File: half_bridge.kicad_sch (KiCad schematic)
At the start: 26 parts, among them Q1 IGC025S08S1, Q2 IGC025S08S1, U16 SN74LVC1G66DCKR, U4 AD8418, U5 LMG1205YFXR, U6 SN74LVC1G66DCKR

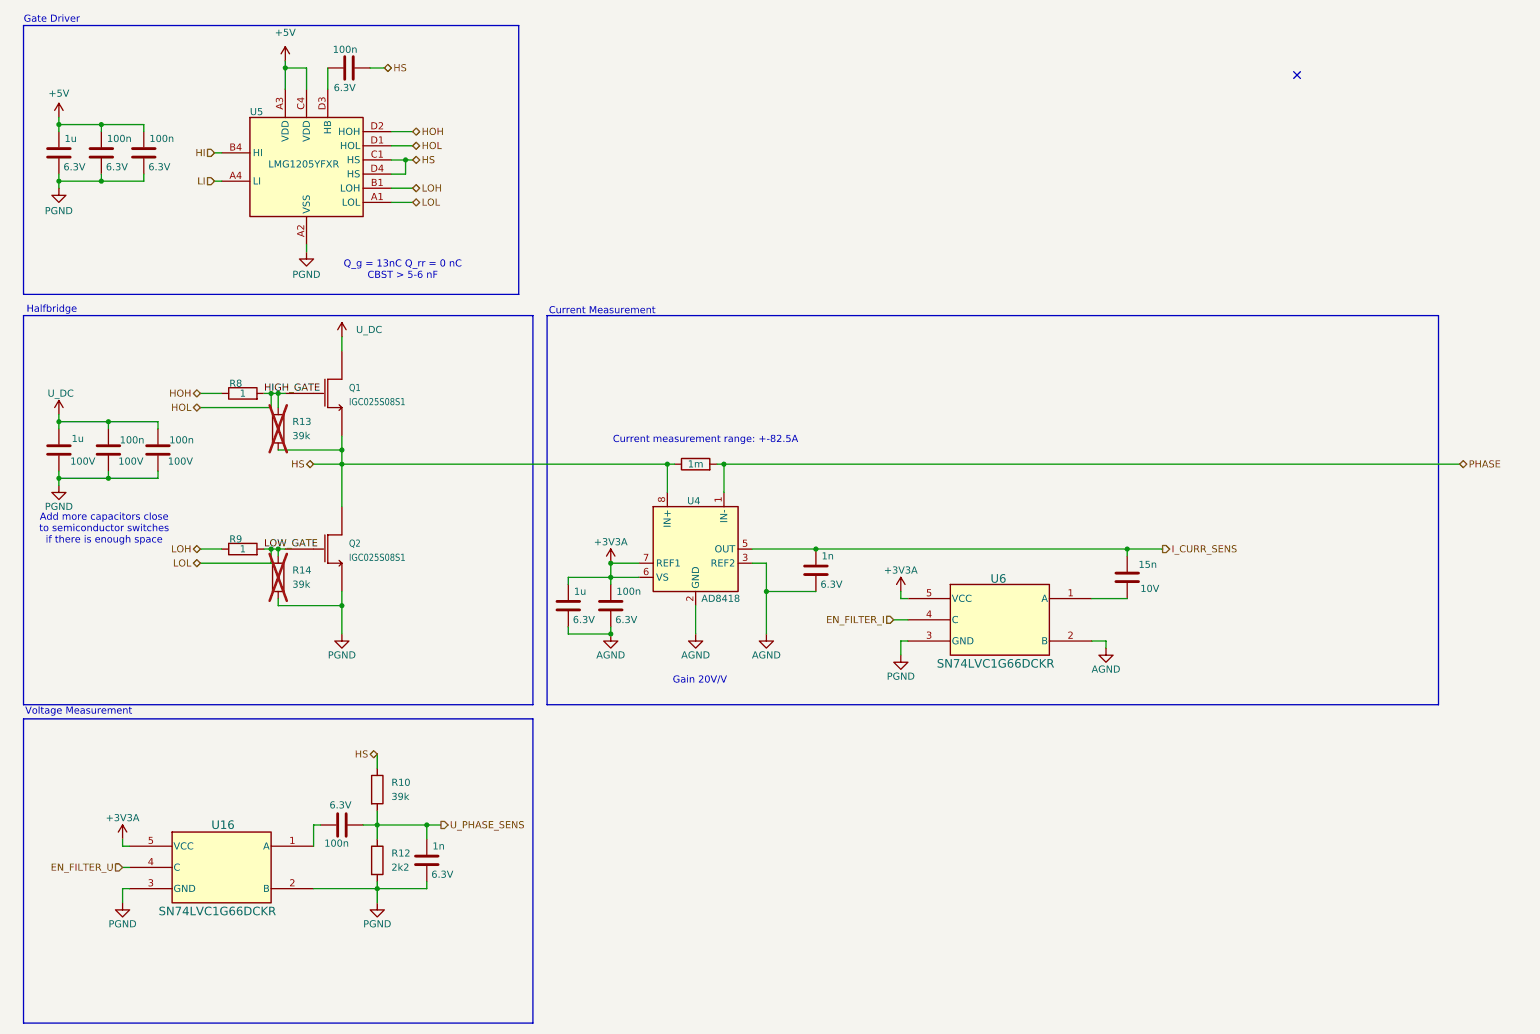
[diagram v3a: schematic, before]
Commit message: added Net Classes  added +5V supply selection header
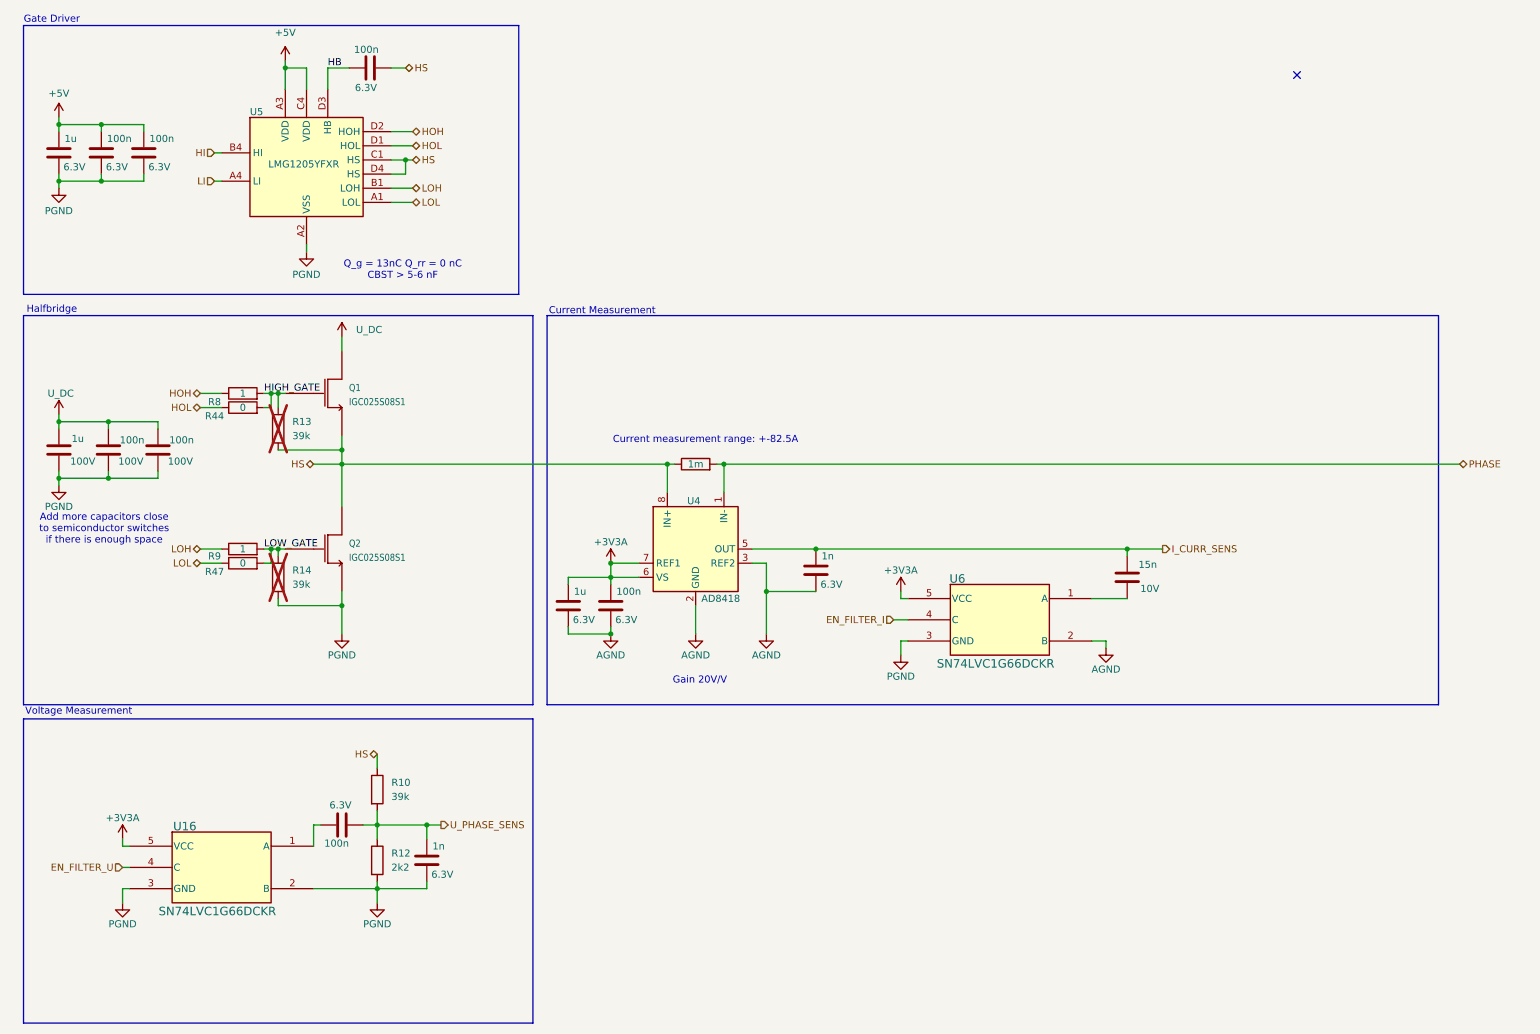
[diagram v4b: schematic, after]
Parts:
- added R44, R47: 0, Resistor_SMD:R_0402_1005Metric, symbol Device:R
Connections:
- net HOL: now also R44.1; no longer Q1.1 (G), R13.1, R8.2
- net LOL: now also R47.1; no longer Q2.1 (G), R14.1, R9.2
- net HB: now reaches C21.1, U5.D3 (HB)
- new net HIGH_GATE: Q1.1 (G), R13.1, R44.2, R8.2
- new net LOW_GATE: Q2.1 (G), R14.1, R47.2, R9.2
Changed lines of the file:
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@@
 	(wire
 		(pts
-			(xy 44.45 83.82) (xy 57.15 83.82)
+			(xy 44.45 83.82) (xy 48.26 83.82)
 		)
 		(stroke
@@
 	(wire
 		(pts
+			(xy 67.31 22.86) (xy 71.12 22.86)
+		)
+		(stroke
+			(width 0)
+			(type default)
+		)
+	)
+	(wire
+		(pts
 			(xy 26.67 33.02) (xy 26.67 34.29)
 		)
@@
 	(wire
 		(pts
+			(xy 55.88 111.76) (xy 57.15 111.76)
+		)
+		(stroke
+			(width 0)
+			(type default)
+		)
+	)
+	(wire
+		(pts
 			(xy 69.85 119.38) (xy 69.85 124.46)
 		)
@@
 	(wire
 		(pts
-			(xy 30.48 162.56) (xy 30.48 161.29)
+			(xy 67.31 22.86) (xy 67.31 26.67)
 		)
 		(stroke
@@
 	(wire
 		(pts
-			(xy 69.85 71.12) (xy 69.85 73.66)
+			(xy 30.48 162.56) (xy 30.48 161.29)
 		)
 		(stroke
@@
 	(wire
 		(pts
-			(xy 143.51 109.22) (xy 154.94 109.22)
+			(xy 69.85 71.12) (xy 69.85 73.66)
 		)
 		(stroke
@@
 	(wire
 		(pts
-			(xy 85.09 168.91) (xy 85.09 170.18)
+			(xy 143.51 109.22) (xy 154.94 109.22)
 		)
 		(stroke
@@
 	(wire
 		(pts
-			(xy 67.31 22.86) (xy 67.31 26.67)
+			(xy 85.09 168.91) (xy 85.09 170.18)
 		)
 		(stroke
@@
 	(wire
 		(pts
-			(xy 44.45 111.76) (xy 57.15 111.76)
+			(xy 44.45 111.76) (xy 48.26 111.76)
 		)
 		(stroke
@@
 	(wire
 		(pts
+			(xy 55.88 83.82) (xy 57.15 83.82)
+		)
+		(stroke
+			(width 0)
+			(type default)
+		)
+	)
+	(wire
+		(pts
 			(xy 34.29 34.29) (xy 34.29 33.02)
 		)
@@
 	(wire
 		(pts
-			(xy 74.93 22.86) (xy 77.47 22.86)
+			(xy 78.74 22.86) (xy 81.28 22.86)
 		)
 		(stroke
@@
 		)
 	)
+	(label "HB"
+		(at 67.31 22.86 0)
+		(effects
+			(font
+				(size 1.27 1.27)
+			)
+			(justify left bottom)
+		)
+	)
 	(label "LOW_GATE"
 		(at 55.88 109.22 0)
@@
 	(hierarchical_label "HS"
 		(shape bidirectional)
-		(at 77.47 22.86 0)
+		(at 81.28 22.86 0)
 		(effects
 			(font
@@
 		(dnp no)
 		(property "Reference" "R9"
-			(at 50.8 107.442 90)
+			(at 46.99 110.49 90)
 			(effects
 				(font
@@
 	(symbol
 		(lib_id "Device:C")
-		(at 71.12 22.86 90)
+		(at 74.93 22.86 90)
 		(unit 1)
 		(exclude_from_sim no)
@@
 		(dnp no)
 		(property "Reference" "C21"
-			(at 69.85 20.32 0)
+			(at 73.66 20.32 0)
 			(effects
 				(font
@@
 		)
 		(property "Value" "100n"
-			(at 72.644 19.558 90)
+			(at 76.454 19.558 90)
 			(effects
 				(font
@@
 		)
 		(property "Footprint" "Capacitor_SMD:C_0402_1005Metric"
-			(at 74.93 21.8948 0)
+			(at 78.74 21.8948 0)
 			(effects
 				(font
@@
 		)
 		(property "Datasheet" "~"
-			(at 71.12 22.86 0)
+			(at 74.93 22.86 0)
 			(effects
 				(font
@@
 		)
 		(property "Description" "100nF 6.3V X7R ±10% 0402 Multilayer Ceramic Capacitors MLCC - SMD/SMT ROHS"
-			(at 71.12 22.86 0)
+			(at 74.93 22.86 0)
 			(effects
 				(font
@@
 		)
 		(property "LCSC" "C424821"
-			(at 71.12 22.86 0)
+			(at 74.93 22.86 0)
 			(effects
 				(font
@@
 		)
 		(property "Voltage Rating" "6.3V"
-			(at 70.358 26.416 90)
+			(at 74.168 26.416 90)
 			(effects
 				(font
@@
 		(dnp no)
 		(property "Reference" "R8"
-			(at 50.8 79.502 90)
+			(at 46.99 82.804 90)
 			(effects
 				(font
@@
 		(dnp no)
 		(property "Reference" "U16"
-			(at 48.514 158.75 0)
+			(at 41.656 159.004 0)
 			(effects
 				(font
@@
 	)
 	(symbol
+		(lib_id "Device:R")
+		(at 52.07 83.82 90)
+		(unit 1)
+		(exclude_from_sim no)
+		(in_bom yes)
+		(on_board yes)
+		(dnp no)
+		(property "Reference" "R44"
+			(at 46.99 85.344 90)
+			(effects
+				(font
+					(size 1.27 1.27)
+				)
+			)
+		)
+		(property "Value" "0"
+			(at 52.07 83.82 90)
+			(effects
+				(font
+					(size 1.27 1.27)
+				)
+			)
+		)
+		(property "Footprint" "Resistor_SMD:R_0402_1005Metric"
+			(at 52.07 85.598 90)
+			(effects
+				(font
+					(size 1.27 1.27)
+				)
+				(hide yes)
+			)
+		)
+		(property "Datasheet" "~"
+			(at 52.07 83.82 0)
+			(effects
+				(font
+					(size 1.27 1.27)
+				)
+				(hide yes)
+			)
+		)
+		(property "Description" "-55℃~+155℃ 0Ω 50V 62.5mW Thick Film Resistor ±1% ±800ppm/℃ 0402 Chip Resistor - Surface Mount ROHS"
+			(at 52.07 83.82 0)
+			(effects
+				(font
+					(size 1.27 1.27)
+				)
+				(hide yes)
+			)
+		)
+		(property "LCSC" "C17168"
+			(at 52.07 83.82 0)
+			(effects
+				(font
+					(size 1.27 1.27)
+				)
+				(hide yes)
+			)
+		)
+		(pin "2"
+		)
+		(pin "1"
+		)
+		(instances
+			(project "NanoGaN"
+				(path "/aa8a494f-605e-4a00-9d3c-daec94709fcb/47075a52-6063-4b82-8884-2b908f359801"
+					(reference "R45")
+					(unit 1)
+				)
+				(path "/aa8a494f-605e-4a00-9d3c-daec94709fcb/6f3a55d2-28c8-407e-8c9d-28f4ee320cbb"
+					(reference "R44")
+					(unit 1)
+				)
+				(path "/aa8a494f-605e-4a00-9d3c-daec94709fcb/e0a1170f-dabd-4224-bbe3-5bcec1b89854"
+					(reference "R46")
+					(unit 1)
+				)
+			)
+		)
+	)
+	(symbol
 		(lib_id "power:+3.3VA")
 		(at 170.18 116.84 0)
@@
 		(dnp no)
 		(property "Reference" "U6"
-			(at 187.706 114.554 0)
+			(at 180.34 114.554 0)
 			(effects
 				(font
@@
 					(unit 1)
 				)
+			)
+		)
+	)
+	(symbol
+		(lib_id "Device:R")
+		(at 52.07 111.76 90)
+		(unit 1)
+		(exclude_from_sim no)
+		(in_bom yes)
+		(on_board yes)
+		(dnp no)
+		(property "Reference" "R47"
+			(at 46.99 113.284 90)
+			(effects
+				(font
+					(size 1.27 1.27)
+				)
+			)
+		)
+		(property "Value" "0"
+			(at 52.07 111.76 90)
+			(effects
+				(font
+					(size 1.27 1.27)
+				)
+			)
+		)
+		(property "Footprint" "Resistor_SMD:R_0402_1005Metric"
+			(at 52.07 113.538 90)
+			(effects
+				(font
+					(size 1.27 1.27)
+				)
+				(hide yes)
+			)
+		)
+		(property "Datasheet" "~"
+			(at 52.07 111.76 0)
+			(effects
+				(font
+					(size 1.27 1.27)
+				)
+				(hide yes)
+			)
+		)
+		(property "Description" "-55℃~+155℃ 0Ω 50V 62.5mW Thick Film Resistor ±1% ±800ppm/℃ 0402 Chip Resistor - Surface Mount ROHS"
+			(at 52.07 111.76 0)
+			(effects
+				(font
+					(size 1.27 1.27)
+				)
+				(hide yes)
+			)
+		)
+		(property "LCSC" "C17168"
+			(at 52.07 111.76 0)
+			(effects
+				(font
+					(size 1.27 1.27)
+				)
+				(hide yes)
+			)
+		)
+		(pin "2"
+		)
+		(pin "1"
+		)
+		(instances
+			(project "NanoGaN"
+				(path "/aa8a494f-605e-4a00-9d3c-daec94709fcb/47075a52-6063-4b82-8884-2b908f359801"
+					(reference "R48")
+					(unit 1)
+				)
+				(path "/aa8a494f-605e-4a00-9d3c-daec94709fcb/6f3a55d2-28c8-407e-8c9d-28f4ee320cbb"
+					(reference "R47")
+					(unit 1)
+				)
+				(path "/aa8a494f-605e-4a00-9d3c-daec94709fcb/e0a1170f-dabd-4224-bbe3-5bcec1b89854"
+					(reference "R49")
+					(unit 1)
+				)

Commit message: added over current protection triggers (adjustable)
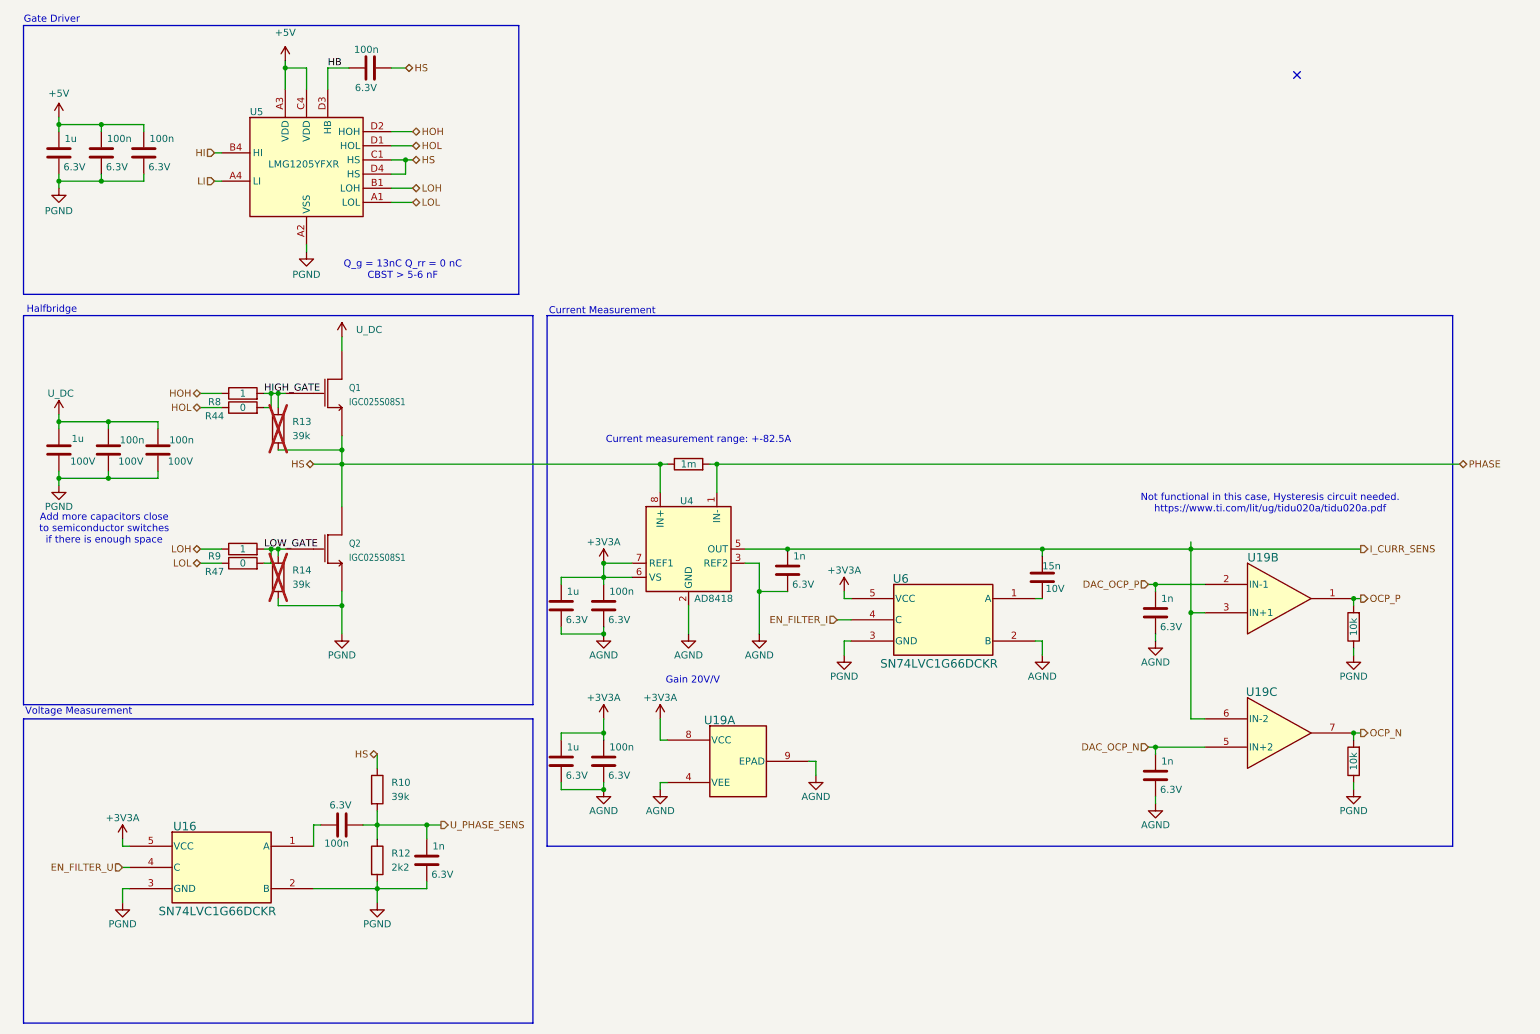
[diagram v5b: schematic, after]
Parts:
- added C100: 1u, Capacitor_SMD:C_0402_1005Metric, symbol Device:C
- added C101: 100n, Capacitor_SMD:C_0402_1005Metric, symbol Device:C
- added C94, C97: 1n, Capacitor_SMD:C_0201_0603Metric, symbol Device:C
- added R51, R54: 10k, Resistor_SMD:R_0402_1005Metric, symbol Device:R
- added U19: NCS2220AMUT1G, NanoGaN:UDFN8_1P6X1P6_ONS, symbol NanoGaN:NCS2220AMUT1G
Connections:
- net +3V3A: now also C100.1, C101.1, U19.8 (VCC)
- net AGND: now also C100.2, C101.2, C94.2, C97.2, U19.4 (VEE), U19.9 (EPAD)
- net I_CURR_SENS: now also U19.3 (IN+1), U19.6 (IN-2)
- net PGND: now also R51.1, R54.1
- new net DAC_OCP_N: C97.1, U19.5 (IN+2)
- new net DAC_OCP_P: C94.1, U19.2 (IN-1)
- new net OCP_N: R54.2, U19.7
- new net OCP_P: R51.2, U19.1
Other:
- note added: "Not functional in this case, Hysteresis circuit needed. https://www.ti.com/lit/ug/tidu020a/tidu020a.pdf"
- moved on the sheet: U4, U6

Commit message: WiP layout
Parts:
- removed C26: 1u, Capacitor_SMD:C_0402_1005Metric, symbol Device:C
- removed R51, R54: 10k, Resistor_SMD:R_0402_1005Metric, symbol Device:R
- added R63, R66: 10k, Resistor_SMD:R_0402_1005Metric, symbol Device:R
- added R69, R72: 39k, Resistor_SMD:R_0603_1608Metric, symbol NanoGaN:R
- R44, R47: value 0 -> 1; LCSC C17168 -> C2077491
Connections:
- net DAC_OCP_N: now also R66.2; no longer U19.5 (IN+2)
- net DAC_OCP_P: now also R63.2; no longer U19.2 (IN-1)
- net I_CURR_SENS: now also U19.2 (IN-1); no longer U19.3 (IN+1)
- net OCP_N: now also R72.2
- net OCP_P: now also R69.2
- new net: R66.1, R72.1, U19.5 (IN+2)
- new net: R63.1, R69.1, U19.3 (IN+1)
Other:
- note added: "See OCP.asc for LTspice sim. of the trigger."
- note added: "V_Hysteresis = (3.3V x 10kohm) / ( 39kohm + 10kohm) = 0.67V"
- note removed: "Not functional in this case, Hysteresis circuit needed. https://www.ti.com/lit/ug/tidu020a/tidu020a.pdf"
- moved on the sheet: U19A, U19B, U19C, U4, U6

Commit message: added the first draft of the layout
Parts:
- removed C100: 1u, Capacitor_SMD:C_0402_1005Metric, symbol Device:C
- removed C101: 100n, Capacitor_SMD:C_0402_1005Metric, symbol Device:C
- removed C90: 15n, Capacitor_SMD:C_0402_1005Metric, symbol Device:C
- removed C94, C97: 1n, Capacitor_SMD:C_0201_0603Metric, symbol Device:C
- removed R11: 1m, NanoGaN:RES_00FEA_VIS-L, symbol Device:R
- removed U16, U6: SN74LVC1G66DCKR, NanoGaN:DCK5, symbol NanoGaN:SN74LVC1G66DCKR
- removed U4: AD8418, Package_SO:SOIC-8_3.9x4.9mm_P1.27mm, symbol Amplifier_Current:AD8418
- added C44: 100n, Capacitor_SMD:C_0805_2012Metric, symbol Device:C
- added C92: 100n, Capacitor_SMD:C_0402_1005Metric, symbol Device:C
- added U4: ACS37030LLZATR-065B3, ACS37030LLZATR020B3, symbol NanoGaN:ACS37030LLZATR-065B3
- C28: value 1n -> 100p; footprint Capacitor_SMD:C_0201_0603Metric -> Capacitor_SMD:C_0402_1005Metric; LCSC C541214 -> C1546
- C87: footprint Capacitor_SMD:C_0201_0603Metric -> Capacitor_SMD:C_0402_1005Metric; LCSC C541214 -> (none); now not fitted; now left out of the parts list
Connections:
- net AGND: now also C92.2; no longer C24.2, C28.2
- net HS: now also U4.1 (IP+)
- net PGND: now also C24.2, C25.2, C28.2, C44.2, U4.3 (GND)
- net PHASE: now also U4.2 (IP-)
- net U_DC: now also C44.1
- net U_PHASE_SENS: no longer C25.2
- net I_CURR_SENS-: now reaches C25.1
- net I_CURR_SENS-: now also U4.4 (VREF)
- net +3V3A renamed +3V3
- net +3V3: now also C92.1, U4.6 (VDD)
- net I_CURR_SENS renamed I_CURR_SENS+
- net I_CURR_SENS+: now also U4.5 (VOUT)
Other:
- note added: "Current measurement range: +-65A"
- note added: "to be later adjusted"
- note removed: "Current measurement range: +-82.5A"
- note removed: "Gain 20V/V"
- moved on the sheet: Q1, Q2, R10, R12, R13, R14, R44, R47, R8, R9, U19A, U19B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
